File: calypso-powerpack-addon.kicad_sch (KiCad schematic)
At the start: 14 parts, among them J1 Conn_02x12_Odd_Even, J2 Conn_02x12_Odd_Even, J3 USB_B_Micro, J4 USB_A_Stacked, J5 USB_A_Stacked, J6 Conn_01x02_Pin, U1 HS8836A, U2 ESP-PSRAM32

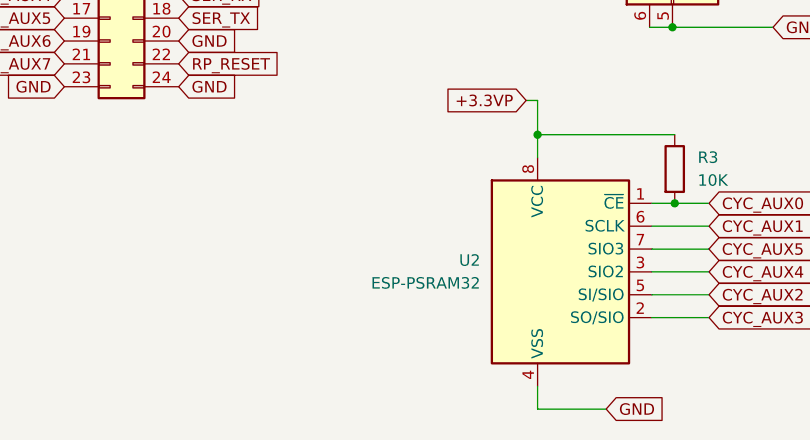
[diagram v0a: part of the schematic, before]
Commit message: Fix PSRAM chip id
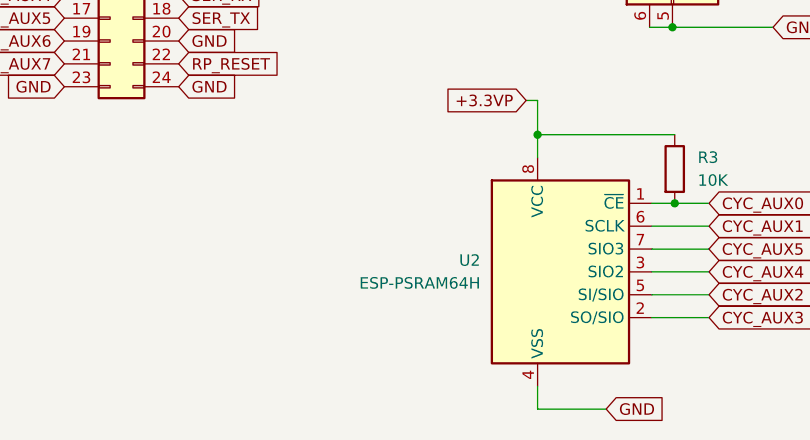
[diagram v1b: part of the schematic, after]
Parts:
- U2: value ESP-PSRAM32 -> ESP-PSRAM64H
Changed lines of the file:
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@@
     (pin "2")
     (instances
-      (project "calypso-usb-addon"
+      (project "calypso-powerpack-addon"
         (path "/e63e39d7-6ac0-4ffd-8aa3-1841a4541b55"
           (reference "C2") (unit 1)
@@
     (pin "2")
     (instances
-      (project "calypso-usb-addon"
+      (project "calypso-powerpack-addon"
         (path "/e63e39d7-6ac0-4ffd-8aa3-1841a4541b55"
           (reference "C3") (unit 1)
@@
     (pin "2")
     (instances
-      (project "calypso-usb-addon"
+      (project "calypso-powerpack-addon"
         (path "/e63e39d7-6ac0-4ffd-8aa3-1841a4541b55"
           (reference "R3") (unit 1)
@@
     (pin "9")
     (instances
-      (project "calypso-usb-addon"
+      (project "calypso-powerpack-addon"
         (path "/e63e39d7-6ac0-4ffd-8aa3-1841a4541b55"
           (reference "J4") (unit 1)
@@
     (pin "2")
     (instances
-      (project "calypso-usb-addon"
+      (project "calypso-powerpack-addon"
         (path "/e63e39d7-6ac0-4ffd-8aa3-1841a4541b55"
           (reference "J6") (unit 1)
@@
     (pin "2")
     (instances
-      (project "calypso-usb-addon"
+      (project "calypso-powerpack-addon"
         (path "/e63e39d7-6ac0-4ffd-8aa3-1841a4541b55"
           (reference "R2") (unit 1)
@@
     (pin "9")
     (instances
-      (project "calypso-usb-addon"
+      (project "calypso-powerpack-addon"
         (path "/e63e39d7-6ac0-4ffd-8aa3-1841a4541b55"
           (reference "J1") (unit 1)
@@
     (pin "2")
     (instances
-      (project "calypso-usb-addon"
+      (project "calypso-powerpack-addon"
         (path "/e63e39d7-6ac0-4ffd-8aa3-1841a4541b55"
           (reference "C1") (unit 1)
@@
     (pin "2")
     (instances
-      (project "calypso-usb-addon"
+      (project "calypso-powerpack-addon"
         (path "/e63e39d7-6ac0-4ffd-8aa3-1841a4541b55"
           (reference "R1") (unit 1)
@@
     (pin "9")
     (instances
-      (project "calypso-usb-addon"
+      (project "calypso-powerpack-addon"
         (path "/e63e39d7-6ac0-4ffd-8aa3-1841a4541b55"
           (reference "U1") (unit 1)
@@
       (effects (font (size 1.27 1.27)) (justify right))
     )
-    (property "Value" "ESP-PSRAM32" (at 92.71 120.65 0)
+    (property "Value" "ESP-PSRAM64H" (at 92.71 120.65 0)
       (effects (font (size 1.27 1.27)) (justify right))
     )
@@
     (pin "5")
     (instances
-      (project "calypso-usb-addon"
+      (project "calypso-powerpack-addon"
         (path "/e63e39d7-6ac0-4ffd-8aa3-1841a4541b55"
           (reference "U2") (unit 1)
@@
     (pin "9")
     (instances
-      (project "calypso-usb-addon"
+      (project "calypso-powerpack-addon"
         (path "/e63e39d7-6ac0-4ffd-8aa3-1841a4541b55"
           (reference "J5") (unit 1)
@@
     (pin "1")
     (instances
-      (project "calypso-usb-addon"
+      (project "calypso-powerpack-addon"
         (path "/e63e39d7-6ac0-4ffd-8aa3-1841a4541b55"
           (reference "#PWR0102") (unit 1)
@@
     (pin "9")
     (instances
-      (project "calypso-usb-addon"
+      (project "calypso-powerpack-addon"
         (path "/e63e39d7-6ac0-4ffd-8aa3-1841a4541b55"
           (reference "J2") (unit 1)
@@
     (pin "1")
     (instances
-      (project "calypso-usb-addon"
+      (project "calypso-powerpack-addon"
         (path "/e63e39d7-6ac0-4ffd-8aa3-1841a4541b55"
           (reference "#PWR0101") (unit 1)
@@
     (pin "6")
     (instances
-      (project "calypso-usb-addon"
+      (project "calypso-powerpack-addon"
         (path "/e63e39d7-6ac0-4ffd-8aa3-1841a4541b55"
           (reference "J3") (unit 1)
